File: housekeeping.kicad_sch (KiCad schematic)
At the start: 44 parts, among them U11 MC34063A, U12 MC34063A, U13 TPS54302

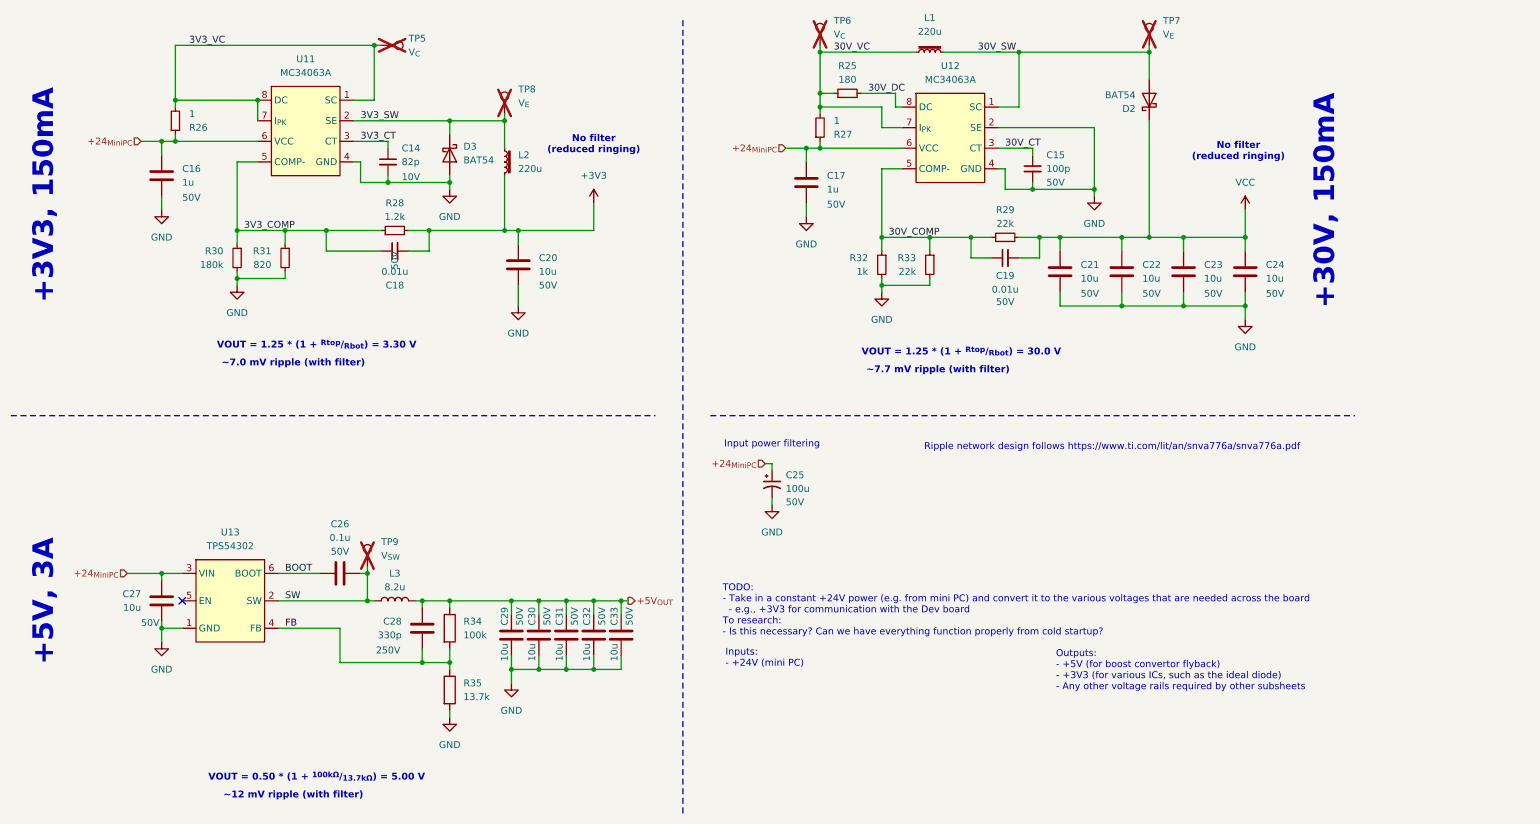
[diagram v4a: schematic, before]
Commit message: Add choice to limit minimum gate voltage to avoid maximum VGS violations
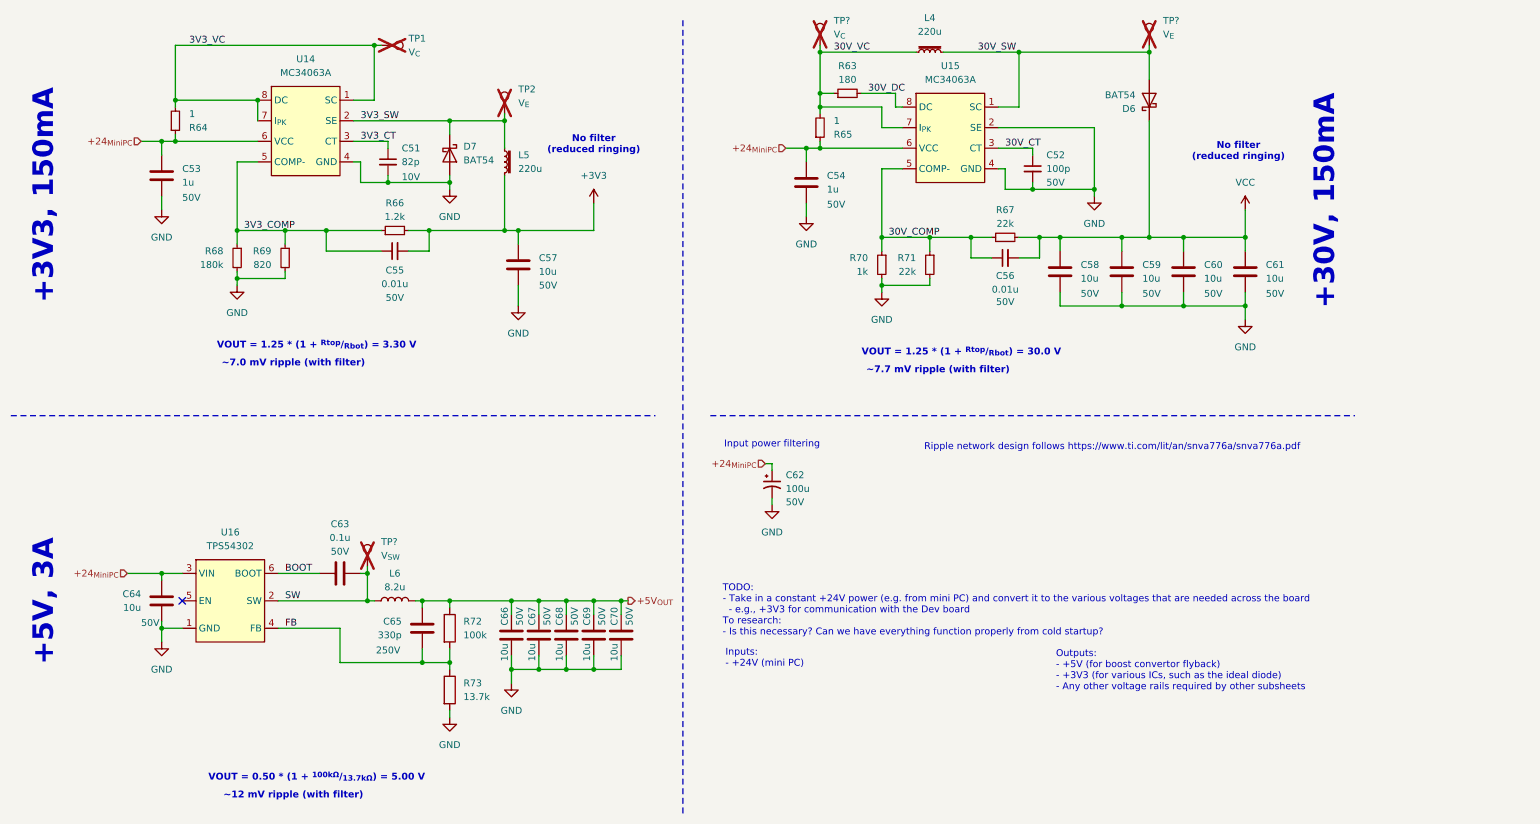
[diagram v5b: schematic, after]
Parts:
- renumbered C14 to C51, C15 to C52, C16 to C53, C17 to C54, C18 to C55, C19 to C56, C20 to C57, C21 to C58, C22 to C59, C23 to C60, C24 to C61, C25 to C62, C26 to C63, C27 to C64, C28 to C65, C29 to C66, C30 to C67, C31 to C68, C32 to C69, C33 to C70, D2 to D6, D3 to D7, L1 to L4, L2 to L5, L3 to L6, R25 to R63, R26 to R64, R27 to R65, R28 to R66, R29 to R67, R30 to R68, R31 to R69, R32 to R70, R33 to R71, R34 to R72, R35 to R73, TP5 to TP1, TP8 to TP2, TP7 to TP?, TP6 to TP?, TP9 to TP?, U11 to U14, U12 to U15, U13 to U16
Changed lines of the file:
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@@
 		(dnp no)
 		(fields_autoplaced yes)
-		(property "Reference" "#PWR093"
+		(property "Reference" "#PWR096"
 			(at 104.14 167.64 0)
 			(effects
@@
 		(dnp no)
 		(fields_autoplaced yes)
-		(property "Reference" "#PWR082"
+		(property "Reference" "#PWR085"
 			(at 130.81 69.85 0)
 			(effects
@@
 		(on_board yes)
 		(dnp no)
-		(property "Reference" "R28"
+		(property "Reference" "R66"
 			(at 93.98 66.04 90)
 			(effects
@@
 		(on_board yes)
 		(dnp no)
-		(property "Reference" "C23"
+		(property "Reference" "C60"
 			(at 243.84 77.4699 0)
 			(effects
@@
 		(on_board yes)
 		(dnp no)
-		(property "Reference" "D2"
+		(property "Reference" "D6"
 			(at 231.14 48.5776 90)
 			(effects
@@
 		(dnp no)
 		(fields_autoplaced yes)
-		(property "Reference" "#PWR087"
+		(property "Reference" "#PWR090"
 			(at 184.15 88.9 0)
 			(effects
@@
 		(dnp no)
 		(fields_autoplaced yes)
-		(property "Reference" "L3"
+		(property "Reference" "L6"
 			(at 93.98 134.62 90)
 			(effects
@@
 		(dnp no)
 		(fields_autoplaced yes)
-		(property "Reference" "#PWR088"
+		(property "Reference" "#PWR091"
 			(at 116.84 91.44 0)
 			(effects
@@
 		(on_board yes)
 		(dnp no)
-		(property "Reference" "C24"
+		(property "Reference" "C61"
 			(at 255.27 77.4699 0)
 			(effects
@@
 		(dnp yes)
 		(fields_autoplaced yes)
-		(property "Reference" "TP7"
+		(property "Reference" "TP?"
 			(at 236.22 32.2579 0)
 			(effects
@@
 		)
 		(instances
+			(project "SupercapManager"
+				(path "/6197145b-e7d4-44cc-9d90-537b6501bf60/2b4de7d2-e111-42d9-afee-f810f96a2f61"
+					(reference "TP?")
+					(unit 1)
+				)
+			)
 			(project "Rev 1B"
 				(path "/e5f99deb-ef42-4c5f-b80a-388477910e20/1e0b2151-e075-4f05-b22a-12d6722ef31a"
@@
 		(dnp no)
 		(fields_autoplaced yes)
-		(property "Reference" "R35"
+		(property "Reference" "R73"
 			(at 106.68 154.9399 0)
 			(effects
@@
 		(on_board yes)
 		(dnp no)
-		(property "Reference" "R26"
+		(property "Reference" "R64"
 			(at 55.88 52.0701 0)
 			(effects
@@
 		(on_board yes)
 		(dnp no)
-		(property "Reference" "C33"
+		(property "Reference" "C70"
 			(at 134.62 144.272 90)
 			(effects
@@
 		(dnp yes)
 		(fields_autoplaced yes)
-		(property "Reference" "TP6"
+		(property "Reference" "TP?"
 			(at 175.26 32.2579 0)
 			(effects
@@
 		)
 		(instances
+			(project "SupercapManager"
+				(path "/6197145b-e7d4-44cc-9d90-537b6501bf60/2b4de7d2-e111-42d9-afee-f810f96a2f61"
+					(reference "TP?")
+					(unit 1)
+				)
+			)
 			(project "Rev 1B"
 				(path "/e5f99deb-ef42-4c5f-b80a-388477910e20/1e0b2151-e075-4f05-b22a-12d6722ef31a"
@@
 		(on_board yes)
 		(dnp no)
-		(property "Reference" "C25"
+		(property "Reference" "C62"
 			(at 166.37 116.4081 0)
 			(effects
@@
 		(dnp no)
 		(fields_autoplaced yes)
-		(property "Reference" "#PWR091"
+		(property "Reference" "#PWR094"
 			(at 50.8 153.67 0)
 			(effects
@@
 		(on_board yes)
 		(dnp no)
-		(property "Reference" "C32"
+		(property "Reference" "C69"
 			(at 129.54 144.272 90)
 			(effects
@@
 		(on_board yes)
 		(dnp no)
-		(property "Reference" "C19"
+		(property "Reference" "C56"
 			(at 207.01 79.502 90)
 			(effects
@@
 		(dnp no)
 		(fields_autoplaced yes)
-		(property "Reference" "#PWR081"
+		(property "Reference" "#PWR084"
 			(at 223.52 71.12 0)
 			(effects
@@
 		(dnp no)
 		(fields_autoplaced yes)
-		(property "Reference" "R34"
+		(property "Reference" "R72"
 			(at 106.68 143.5099 0)
 			(effects
@@
 		(dnp no)
 		(fields_autoplaced yes)
-		(property "Reference" "U12"
+		(property "Reference" "U15"
 			(at 196.85 40.64 0)
 			(effects
@@
 		(dnp yes)
 		(fields_autoplaced yes)
-		(property "Reference" "TP5"
+		(property "Reference" "TP1"
 			(at 96.52 35.5599 90)
 			(effects
@@
 		(on_board yes)
 		(dnp no)
-		(property "Reference" "R29"
+		(property "Reference" "R67"
 			(at 207.01 67.31 90)
 			(effects
@@
 		(on_board yes)
 		(dnp no)
-		(property "Reference" "D3"
+		(property "Reference" "D7"
 			(at 106.68 55.5624 90)
 			(effects
@@
 		(dnp no)
 		(fields_autoplaced yes)
-		(property "Reference" "#PWR089"
+		(property "Reference" "#PWR092"
 			(at 251.46 93.98 0)
 			(effects
@@
 		(dnp no)
 		(fields_autoplaced yes)
-		(property "Reference" "#PWR092"
+		(property "Reference" "#PWR095"
 			(at 115.57 161.29 0)
 			(effects
@@
 		(on_board yes)
 		(dnp no)
-		(property "Reference" "C14"
+		(property "Reference" "C51"
 			(at 95.25 55.88 0)
 			(effects
@@
 		(on_board yes)
 		(dnp no)
-		(property "Reference" "C29"
+		(property "Reference" "C66"
 			(at 114.3 144.272 90)
 			(effects
@@
 		(dnp no)
 		(fields_autoplaced yes)
-		(property "Reference" "#PWR085"
+		(property "Reference" "#PWR088"
 			(at 170.18 74.93 0)
 			(effects
@@
 		(dnp no)
 		(fields_autoplaced yes)
-		(property "Reference" "#PWR090"
+		(property "Reference" "#PWR093"
 			(at 163.83 128.27 0)
 			(effects
@@
 		(on_board yes)
 		(dnp no)
-		(property "Reference" "R25"
+		(property "Reference" "R63"
 			(at 177.8 40.64 90)
 			(effects
@@
 		(dnp no)
 		(fields_autoplaced yes)
-		(property "Reference" "#PWR080"
+		(property "Reference" "#PWR083"
 			(at 104.14 69.85 0)
 			(effects
@@
 		(on_board yes)
 		(dnp no)
-		(property "Reference" "R31"
+		(property "Reference" "R69"
 			(at 71.12 74.9299 0)
 			(effects
@@
 		(on_board yes)
 		(dnp no)
-		(property "Reference" "C21"
+		(property "Reference" "C58"
 			(at 220.98 77.4699 0)
 			(effects
@@
 		(on_board yes)
 		(dnp no)
-		(property "Reference" "C22"
+		(property "Reference" "C59"
 			(at 232.41 77.4699 0)
 			(effects
@@
 		(dnp no)
 		(fields_autoplaced yes)
-		(property "Reference" "L1"
+		(property "Reference" "L4"
 			(at 193.04 31.75 90)
 			(effects
@@
 		(dnp no)
 		(fields_autoplaced yes)
-		(property "Reference" "#PWR086"
+		(property "Reference" "#PWR089"
 			(at 64.77 87.63 0)
 			(effects
@@
 		(dnp no)
 		(fields_autoplaced yes)
-		(property "Reference" "U11"
+		(property "Reference" "U14"
 			(at 77.47 39.37 0)
 			(effects
@@
 		(on_board yes)
 		(dnp no)
-		(property "Reference" "R27"
+		(property "Reference" "R65"
 			(at 175.26 53.3401 0)
 			(effects
@@
 		(dnp no)
 		(fields_autoplaced yes)
-		(property "Reference" "#PWR084"
+		(property "Reference" "#PWR087"
 			(at 251.46 71.12 0)
 			(effects
@@
 		(on_board yes)
 		(dnp no)
-		(property "Reference" "C27"
+		(property "Reference" "C64"
 			(at 46.99 138.4299 0)
 			(effects
@@
 		(on_board yes)
 		(dnp no)
-		(property "Reference" "C20"
+		(property "Reference" "C57"
 			(at 120.65 76.1999 0)
 			(effects
@@
 		(on_board yes)
 		(dnp no)
-		(property "Reference" "C28"
+		(property "Reference" "C65"
 			(at 95.25 143.5099 0)
 			(effects
@@
 		(on_board yes)
 		(dnp no)
-		(property "Reference" "C17"
+		(property "Reference" "C54"
 			(at 173.99 60.9599 0)
 			(effects
@@
 		(on_board yes)
 		(dnp no)
-		(property "Reference" "C26"
+		(property "Reference" "C63"
 			(at 83.82 125.476 90)
 			(effects
@@
 		(on_board yes)
 		(dnp no)
-		(property "Reference" "C31"
+		(property "Reference" "C68"
 			(at 124.46 144.272 90)
 			(effects
@@
 		(dnp no)
 		(fields_autoplaced yes)
-		(property "Reference" "L2"
+		(property "Reference" "L5"
 			(at 116.84 57.1499 0)
 			(effects
@@
 		(dnp no)
 		(fields_autoplaced yes)
-		(property "Reference" "U13"
+		(property "Reference" "U16"
 			(at 63.5 127 0)
 			(effects
@@
 		(on_board yes)
 		(dnp no)
-		(property "Reference" "R33"
+		(property "Reference" "R71"
 			(at 190.5 76.1999 0)
 			(effects
@@
 		(dnp no)
 		(fields_autoplaced yes)
-		(property "Reference" "#PWR083"
+		(property "Reference" "#PWR086"
 			(at 50.8 73.66 0)
 			(effects
@@
 		(on_board yes)
 		(dnp no)
-		(property "Reference" "R30"
+		(property "Reference" "R68"
 			(at 62.23 74.9299 0)
 			(effects
@@
 		(on_board yes)
 		(dnp no)
-		(property "Reference" "C30"
+		(property "Reference" "C67"
 			(at 119.38 144.272 90)
 			(effects
@@
 		(on_board yes)
 		(dnp no)
-		(property "Reference" "R32"
+		(property "Reference" "R70"
 			(at 181.61 76.1999 0)
 			(effects
@@
 		(on_board yes)
 		(dnp no)
-		(property "Reference" "C18"
-			(at 93.9863 81.28 90)
+		(property "Reference" "C55"
+			(at 93.98 78.486 90)
 			(effects
 				(font
@@
 		)
 		(property "Value" "0.01u"
-			(at 93.9863 78.74 90)
+			(at 93.98 81.026 90)
 			(effects
 				(font
@@
 		)
 		(property "Voltage Rating" "50V"
-			(at 93.98 74.93 0)
+			(at 93.98 83.566 90)
 			(effects
 				(font
 					(size 1.27 1.27)
 				)
-				(justify left)
 			)
 		)
@@
 		(dnp yes)
 		(fields_autoplaced yes)
-		(property "Reference" "TP9"
+		(property "Reference" "TP?"
 			(at 91.44 128.7779 0)
 			(effects
@@
 		)
 		(instances
+			(project "SupercapManager"
+				(path "/6197145b-e7d4-44cc-9d90-537b6501bf60/2b4de7d2-e111-42d9-afee-f810f96a2f61"
+					(reference "TP?")
+					(unit 1)
+				)
+			)
 			(project "Rev 1B"
 				(path "/e5f99deb-ef42-4c5f-b80a-388477910e20/1e0b2151-e075-4f05-b22a-12d6722ef31a"
@@
 		(on_board yes)
 		(dnp no)
-		(property "Reference" "C16"
+		(property "Reference" "C53"
 			(at 54.61 59.6899 0)
 			(effects
@@
 		(on_board yes)
 		(dnp no)
-		(property "Reference" "C15"
+		(property "Reference" "C52"
 			(at 214.63 57.15 0)
 			(effects
@@
 		(dnp yes)
 		(fields_autoplaced yes)
-		(property "Reference" "TP8"
+		(property "Reference" "TP2"
 			(at 116.84 44.9579 0)
 			(effects

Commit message: Completed preliminary layout
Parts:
- gave numbers to parts that had none: 3
- renumbered C51 to C14, C52 to C15, C53 to C16, C54 to C17, C55 to C18, C56 to C19, C57 to C20, C58 to C21, C59 to C22, C60 to C23, C61 to C24, C62 to C25, C63 to C26, C64 to C27, C65 to C28, C66 to C29, C67 to C30, C68 to C31, C69 to C32, C70 to C33, D6 to D2, D7 to D3, L4 to L1, L5 to L2, L6 to L3, R63 to R25, R64 to R26, R65 to R27, R66 to R28, R67 to R29, R68 to R30, R69 to R31, R70 to R32, R71 to R33, R72 to R34, R73 to R35, TP1 to TP5, TP2 to TP8, U14 to U11, U15 to U12, U16 to U13
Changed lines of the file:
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@@
 		(dnp no)
 		(fields_autoplaced yes)
-		(property "Reference" "#PWR096"
+		(property "Reference" "#PWR093"
 			(at 104.14 167.64 0)
 			(effects
@@
 		(dnp no)
 		(fields_autoplaced yes)
-		(property "Reference" "#PWR085"
+		(property "Reference" "#PWR082"
 			(at 130.81 69.85 0)
 			(effects
@@
 		(on_board yes)
 		(dnp no)
-		(property "Reference" "R66"
+		(property "Reference" "R28"
 			(at 93.98 66.04 90)
 			(effects
@@
 		(on_board yes)
 		(dnp no)
-		(property "Reference" "C60"
+		(property "Reference" "C23"
 			(at 243.84 77.4699 0)
 			(effects
@@
 		(on_board yes)
 		(dnp no)
-		(property "Reference" "D6"
+		(property "Reference" "D2"
 			(at 231.14 48.5776 90)
 			(effects
@@
 		(dnp no)
 		(fields_autoplaced yes)
-		(property "Reference" "#PWR090"
+		(property "Reference" "#PWR087"
 			(at 184.15 88.9 0)
 			(effects
@@
 		(dnp no)
 		(fields_autoplaced yes)
-		(property "Reference" "L6"
+		(property "Reference" "L3"
 			(at 93.98 134.62 90)
 			(effects
@@
 		(dnp no)
 		(fields_autoplaced yes)
-		(property "Reference" "#PWR091"
+		(property "Reference" "#PWR088"
 			(at 116.84 91.44 0)
 			(effects
@@
 		(on_board yes)
 		(dnp no)
-		(property "Reference" "C61"
+		(property "Reference" "C24"
 			(at 255.27 77.4699 0)
 			(effects
@@
 		(dnp yes)
 		(fields_autoplaced yes)
-		(property "Reference" "TP?"
+		(property "Reference" "TP7"
 			(at 236.22 32.2579 0)
 			(effects
@@
 		(dnp no)
 		(fields_autoplaced yes)
-		(property "Reference" "R73"
+		(property "Reference" "R35"
 			(at 106.68 154.9399 0)
 			(effects
@@
 		(on_board yes)
 		(dnp no)
-		(property "Reference" "R64"
+		(property "Reference" "R26"
 			(at 55.88 52.0701 0)
 			(effects
@@
 		(on_board yes)
 		(dnp no)
-		(property "Reference" "C70"
+		(property "Reference" "C33"
 			(at 134.62 144.272 90)
 			(effects
@@
 		(dnp yes)
 		(fields_autoplaced yes)
-		(property "Reference" "TP?"
+		(property "Reference" "TP6"
 			(at 175.26 32.2579 0)
 			(effects
@@
 		(on_board yes)
 		(dnp no)
-		(property "Reference" "C62"
+		(property "Reference" "C25"
 			(at 166.37 116.4081 0)
 			(effects
@@
 		(dnp no)
 		(fields_autoplaced yes)
-		(property "Reference" "#PWR094"
+		(property "Reference" "#PWR091"
 			(at 50.8 153.67 0)
 			(effects
@@
 		(on_board yes)
 		(dnp no)
-		(property "Reference" "C69"
+		(property "Reference" "C32"
 			(at 129.54 144.272 90)
 			(effects
@@
 		(on_board yes)
 		(dnp no)
-		(property "Reference" "C56"
+		(property "Reference" "C19"
 			(at 207.01 79.502 90)
 			(effects
@@
 		(dnp no)
 		(fields_autoplaced yes)
-		(property "Reference" "#PWR084"
+		(property "Reference" "#PWR081"
 			(at 223.52 71.12 0)
 			(effects
@@
 		(dnp no)
 		(fields_autoplaced yes)
-		(property "Reference" "R72"
+		(property "Reference" "R34"
 			(at 106.68 143.5099 0)
 			(effects
@@
 		(dnp no)
 		(fields_autoplaced yes)
-		(property "Reference" "U15"
+		(property "Reference" "U12"
 			(at 196.85 40.64 0)
 			(effects
@@
 		(dnp yes)
 		(fields_autoplaced yes)
-		(property "Reference" "TP1"
+		(property "Reference" "TP5"
 			(at 96.52 35.5599 90)
 			(effects
@@
 		(on_board yes)
 		(dnp no)
-		(property "Reference" "R67"
+		(property "Reference" "R29"
 			(at 207.01 67.31 90)
 			(effects
@@
 		(on_board yes)
 		(dnp no)
-		(property "Reference" "D7"
+		(property "Reference" "D3"
 			(at 106.68 55.5624 90)
 			(effects
@@
 		(dnp no)
 		(fields_autoplaced yes)
-		(property "Reference" "#PWR092"
+		(property "Reference" "#PWR089"
 			(at 251.46 93.98 0)
 			(effects
@@
 		(dnp no)
 		(fields_autoplaced yes)
-		(property "Reference" "#PWR095"
+		(property "Reference" "#PWR092"
 			(at 115.57 161.29 0)
 			(effects
@@
 		(on_board yes)
 		(dnp no)
-		(property "Reference" "C51"
+		(property "Reference" "C14"
 			(at 95.25 55.88 0)
 			(effects
@@
 		(on_board yes)
 		(dnp no)
-		(property "Reference" "C66"
+		(property "Reference" "C29"
 			(at 114.3 144.272 90)
 			(effects
@@
 		(dnp no)
 		(fields_autoplaced yes)
-		(property "Reference" "#PWR088"
+		(property "Reference" "#PWR085"
 			(at 170.18 74.93 0)
 			(effects
@@
 		(dnp no)
 		(fields_autoplaced yes)
-		(property "Reference" "#PWR093"
+		(property "Reference" "#PWR090"
 			(at 163.83 128.27 0)
 			(effects
@@
 		(on_board yes)
 		(dnp no)
-		(property "Reference" "R63"
+		(property "Reference" "R25"
 			(at 177.8 40.64 90)
 			(effects
@@
 		(dnp no)
 		(fields_autoplaced yes)
-		(property "Reference" "#PWR083"
+		(property "Reference" "#PWR080"
 			(at 104.14 69.85 0)
 			(effects
@@
 		(on_board yes)
 		(dnp no)
-		(property "Reference" "R69"
+		(property "Reference" "R31"
 			(at 71.12 74.9299 0)
 			(effects
@@
 		(on_board yes)
 		(dnp no)
-		(property "Reference" "C58"
+		(property "Reference" "C21"
 			(at 220.98 77.4699 0)
 			(effects
@@
 		(on_board yes)
 		(dnp no)
-		(property "Reference" "C59"
+		(property "Reference" "C22"
 			(at 232.41 77.4699 0)
 			(effects
@@
 		(dnp no)
 		(fields_autoplaced yes)
-		(property "Reference" "L4"
+		(property "Reference" "L1"
 			(at 193.04 31.75 90)
 			(effects
@@
 		(dnp no)
 		(fields_autoplaced yes)
-		(property "Reference" "#PWR089"
+		(property "Reference" "#PWR086"
 			(at 64.77 87.63 0)
 			(effects
@@
 		(dnp no)
 		(fields_autoplaced yes)
-		(property "Reference" "U14"
+		(property "Reference" "U11"
 			(at 77.47 39.37 0)
 			(effects
@@
 		(on_board yes)
 		(dnp no)
-		(property "Reference" "R65"
+		(property "Reference" "R27"
 			(at 175.26 53.3401 0)
 			(effects
@@
 		(dnp no)
 		(fields_autoplaced yes)
-		(property "Reference" "#PWR087"
+		(property "Reference" "#PWR084"
 			(at 251.46 71.12 0)
 			(effects
@@
 		(on_board yes)
 		(dnp no)
-		(property "Reference" "C64"
+		(property "Reference" "C27"
 			(at 46.99 138.4299 0)
 			(effects
@@
 		(on_board yes)
 		(dnp no)
-		(property "Reference" "C57"
+		(property "Reference" "C20"
 			(at 120.65 76.1999 0)
 			(effects
@@
 		(on_board yes)
 		(dnp no)
-		(property "Reference" "C65"
+		(property "Reference" "C28"
 			(at 95.25 143.5099 0)
 			(effects
@@
 		(on_board yes)
 		(dnp no)
-		(property "Reference" "C54"
+		(property "Reference" "C17"
 			(at 173.99 60.9599 0)
 			(effects
@@
 		(on_board yes)
 		(dnp no)
-		(property "Reference" "C63"
+		(property "Reference" "C26"
 			(at 83.82 125.476 90)
 			(effects
@@
 		(on_board yes)
 		(dnp no)
-		(property "Reference" "C68"
+		(property "Reference" "C31"
 			(at 124.46 144.272 90)
 			(effects
@@
 		(dnp no)
 		(fields_autoplaced yes)
-		(property "Reference" "L5"
+		(property "Reference" "L2"
 			(at 116.84 57.1499 0)
 			(effects
@@
 		(dnp no)
 		(fields_autoplaced yes)
-		(property "Reference" "U16"
+		(property "Reference" "U13"
 			(at 63.5 127 0)
 			(effects
@@
 		(on_board yes)
 		(dnp no)
-		(property "Reference" "R71"
+		(property "Reference" "R33"
 			(at 190.5 76.1999 0)
 			(effects
@@
 		(dnp no)
 		(fields_autoplaced yes)
-		(property "Reference" "#PWR086"
+		(property "Reference" "#PWR083"
 			(at 50.8 73.66 0)
 			(effects
@@
 		(on_board yes)
 		(dnp no)
-		(property "Reference" "R68"
+		(property "Reference" "R30"
 			(at 62.23 74.9299 0)
 			(effects
@@
 		(on_board yes)
 		(dnp no)
-		(property "Reference" "C67"
+		(property "Reference" "C30"
 			(at 119.38 144.272 90)
 			(effects
@@
 		(on_board yes)
 		(dnp no)
-		(property "Reference" "R70"
+		(property "Reference" "R32"
 			(at 181.61 76.1999 0)
 			(effects
@@
 		(on_board yes)
 		(dnp no)
-		(property "Reference" "C55"
+		(property "Reference" "C18"
 			(at 93.98 78.486 90)
 			(effects
@@
 		(dnp yes)
 		(fields_autoplaced yes)
-		(property "Reference" "TP?"
+		(property "Reference" "TP9"
 			(at 91.44 128.7779 0)
 			(effects
@@
 		(on_board yes)
 		(dnp no)
-		(property "Reference" "C53"
+		(property "Reference" "C16"
 			(at 54.61 59.6899 0)
 			(effects
@@
 		(on_board yes)
 		(dnp no)
-		(property "Reference" "C52"
+		(property "Reference" "C15"
 			(at 214.63 57.15 0)
 			(effects
@@
 		(dnp yes)
 		(fields_autoplaced yes)
-		(property "Reference" "TP2"
+		(property "Reference" "TP8"
 			(at 116.84 44.9579 0)
 			(effects
